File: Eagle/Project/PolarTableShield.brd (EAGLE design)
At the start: 56 x 59.7 mm, 48 parts, among them IC1 74AHC1G86DBV, IC2 LM358D, J1 Pi Power Jack, J10 LED + Radio, J2 Header - Right angled, female, J3 Pi Connection, J5 IR Sensors, J6 Switch A + B, J7 Switch C + D, J8 Switch E + F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

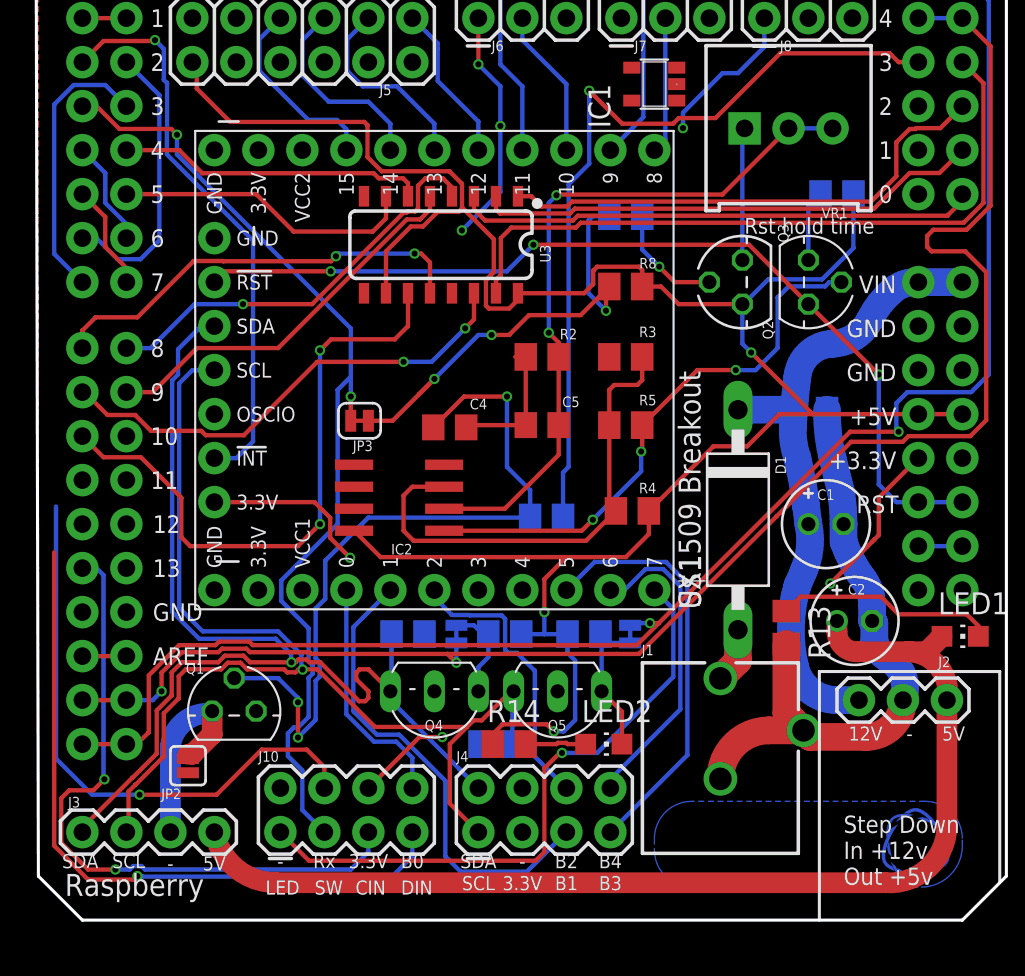
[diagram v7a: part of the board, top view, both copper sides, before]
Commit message: Moved the pins to be more efficient.
Put the rotory encoder signals onto D8 & D9 so they are on digital pin bank B in the lowest two bits. This can save a cycle shifting the data into position.
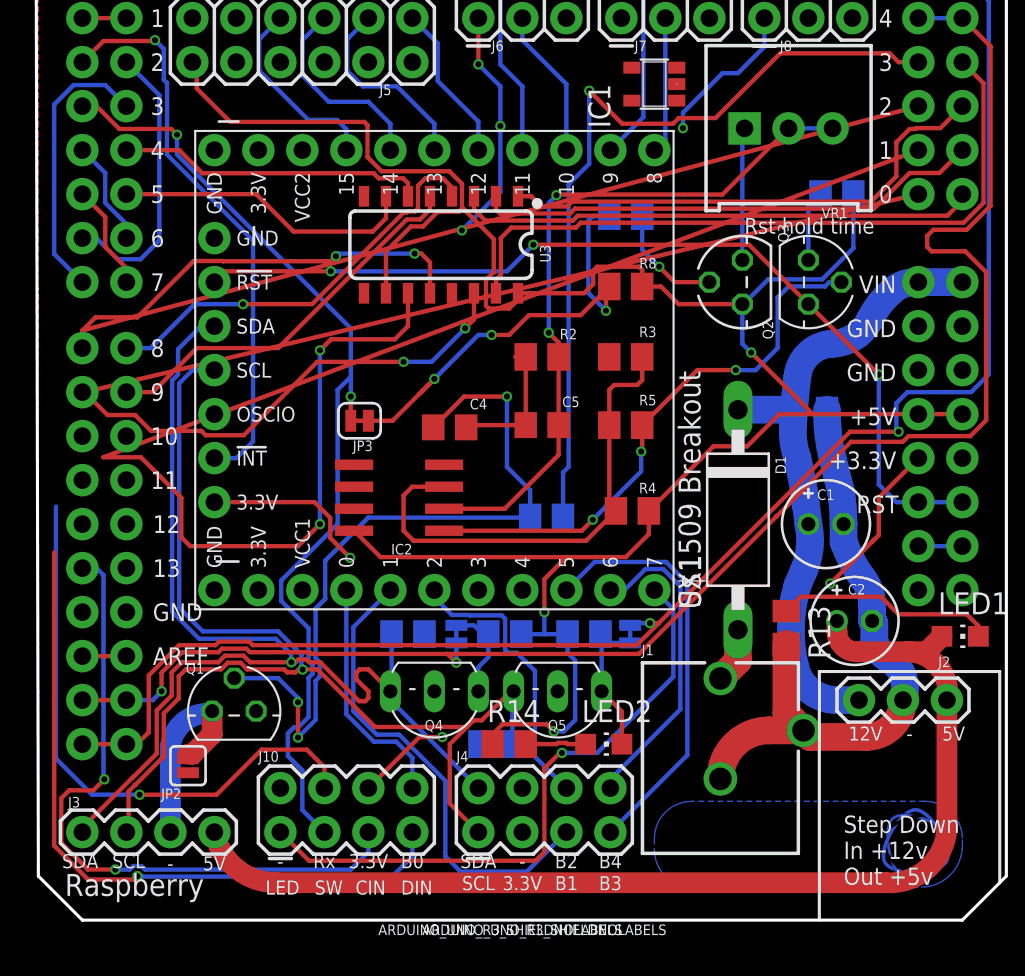
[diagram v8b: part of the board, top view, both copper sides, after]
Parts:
- B1, B2: value (none) -> ARDUINO_UNO_R3_SHIELDNOLABELS
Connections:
- net D11_SDIN renamed SDIN
- net D12_RXDATA renamed RXDATA
- net D13_SCIN renamed SCIN
- removed net A0_SW_E: B1.A0, IC1.1, J8.3
- removed net A1_SW_F: B1.A1, IC1.2, J8.4
- removed net A2_WAKE_SW: B1.A2, B1.D3, IC1.4, J10.3, JP3.1
- new net SW_E: B1.D8, IC1.1, J8.3
- new net SW_F: B1.D9, IC1.2, J8.4
- new net WAKE_SW: B1.D10, B1.D3, IC1.4, J10.3, JP3.1
- net CLK: now also B1.A1; no longer B1.D10
- net DATA: now also B1.A0; no longer B1.D9
- net LATCH: now also B1.A2; no longer B1.D8
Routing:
- net WAKE_SW: track 0.00 -> 56.3 mm, vias 0 -> 2
- net A2_WAKE_SW: track 56.3 -> 0.00 mm, vias 2 -> 0
- net DATA: track 27.9 -> 77.3 mm
- net LATCH: track 24.9 -> 73.9 mm
- net CLK: track 35.8 -> 84.3 mm
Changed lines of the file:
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@@
 </autorouter>
 <elements>
-<element name="B1" library="keir_library" package="UNO_R3_SHIELD_NOLABELS" package3d_urn="urn:adsk.eagle:package:37324/1" value="" x="26.67" y="30.48"/>
+<element name="B1" library="keir_library" package="UNO_R3_SHIELD_NOLABELS" package3d_urn="urn:adsk.eagle:package:37324/1" value="ARDUINO_UNO_R3_SHIELDNOLABELS" x="26.67" y="30.48"/>
 <element name="J1" library="SparkFun-Connectors" library_urn="urn:adsk.eagle:library:513" package="POWER_JACK_PTH_BREAD" package3d_urn="urn:adsk.eagle:package:38228/1" value="Pi Power Jack" x="39.37" y="0.254">
 <attribute name="NAME" x="34.8234" y="15.2908" size="0.6096" layer="25" font="vector" ratio="18"/>
@@
 <attribute name="VALUE" x="29.718" y="21.59" size="0.6" layer="28" font="vector" ratio="18" rot="MR0"/>
 </element>
-<element name="B2" library="keir_library" package="UNO_R3_SHIELD_NOLABELS" package3d_urn="urn:adsk.eagle:package:37324/1" value="" x="29.21" y="30.48"/>
+<element name="B2" library="keir_library" package="UNO_R3_SHIELD_NOLABELS" package3d_urn="urn:adsk.eagle:package:37324/1" value="ARDUINO_UNO_R3_SHIELDNOLABELS" x="29.21" y="30.48"/>
 <element name="C4" library="resistor" library_urn="urn:adsk.eagle:library:348" package="C0805" package3d_urn="urn:adsk.eagle:package:23617/2" value="100nF" x="23.749" y="28.448">
 <attribute name="NAME" x="25.908" y="30.099" size="0.6096" layer="25" font="vector" ratio="18" rot="R180"/>
@@
 <wire x1="29.3497" y1="11.303" x2="29.7561" y2="10.8966" width="0.254" layer="1"/>
 </signal>
-<signal name="A2_WAKE_SW" class="4">
+<signal name="WAKE_SW" class="4">
 <contactref element="J10" pad="3"/>
 <contactref element="JP3" pad="1"/>
@@
 <wire x1="14.4046" y1="10.781825" x2="14.4046" y2="9.4714" width="0.254" layer="16"/>
 <wire x1="15.5956" y1="13.9830625" x2="15.5956" y2="11.7253375" width="0.254" layer="16"/>
-<contactref element="B1" pad="A2"/>
 <contactref element="B1" pad="D3"/>
 <contactref element="IC1" pad="4"/>
-<wire x1="34.26" y1="49.21" x2="50.8" y2="46.99" width="0" layer="19" extent="1-1"/>
+<wire x1="34.26" y1="49.21" x2="2.54" y2="27.94" width="0" layer="19" extent="1-1"/>
 <wire x1="18.034" y1="34.163" x2="34.26" y2="49.21" width="0" layer="19" extent="1-16"/>
 <wire x1="2.54" y1="46.99" x2="3.3557875" y2="46.99" width="0" layer="19" extent="1-1"/>
+<contactref element="B1" pad="D10"/>
 </signal>
 <signal name="PI_GROUND" class="2">
@@
 <signal name="CLK" class="4">
 <contactref element="U3" pad="11"/>
-<contactref element="B1" pad="D10"/>
-<wire x1="2.54" y1="27.94" x2="3.7592" y2="26.7208" width="0.254" layer="1"/>
+<wire x1="50.8" y1="44.45" x2="3.7592" y2="26.7208" width="0.254" layer="1"/>
 <wire x1="8.255" y1="24.384" x2="8.255" y2="22.098" width="0.254" layer="1"/>
 <wire x1="5.9182" y1="26.7208" x2="8.255" y2="24.384" width="0.254" layer="1"/>
@@
 <via x="16.256" y="32.893" extent="1-16" drill="0.35"/>
 <wire x1="20.574" y1="33.528" x2="16.891" y2="33.528" width="0.254" layer="1"/>
+<contactref element="B1" pad="A1"/>
 </signal>
 <signal name="XSTEP" class="4">
@@
 <signal name="LATCH" class="4">
 <contactref element="U3" pad="12"/>
-<contactref element="B1" pad="D8"/>
 <wire x1="22.606" y1="36.189" x2="22.606" y2="37.973" width="0.254" layer="1"/>
 <wire x1="22.606" y1="37.973" x2="22.098" y2="38.481" width="0.254" layer="1"/>
 <wire x1="22.098" y1="38.481" x2="21.717" y2="38.481" width="0.254" layer="1"/>
-<wire x1="2.54" y1="33.02" x2="2.54" y2="34.036" width="0.254" layer="1"/>
+<wire x1="50.8" y1="46.99" x2="2.54" y2="34.036" width="0.254" layer="1"/>
 <wire x1="2.54" y1="34.036" x2="3.302" y2="34.798" width="0.254" layer="1"/>
 <wire x1="5.715" y1="34.798" x2="3.302" y2="34.798" width="0.254" layer="1"/>
@@
 <wire x1="21.717" y1="38.481" x2="17.332225" y2="38.481" width="0.254" layer="16"/>
 <wire x1="17.332225" y1="38.481" x2="17.1751125" y2="38.3238875" width="0.254" layer="16"/>
+<contactref element="B1" pad="A2"/>
 </signal>
 <signal name="DATA" class="4">
 <contactref element="U3" pad="14"/>
-<contactref element="B1" pad="D9"/>
 <wire x1="6.4994125" y1="28.2448" x2="5.5850125" y2="29.1592" width="0.254" layer="1"/>
-<wire x1="2.667" y1="30.48" x2="2.54" y2="30.48" width="0.254" layer="1"/>
+<wire x1="2.667" y1="30.48" x2="50.8" y2="41.91" width="0.254" layer="1"/>
 <wire x1="25.146" y1="36.189" x2="25.146" y2="34.671" width="0.254" layer="1"/>
 <wire x1="5.5850125" y1="29.1592" x2="3.9878" y2="29.1592" width="0.254" layer="1"/>
@@
 <wire x1="24.638" y1="34.163" x2="22.7028875" y2="32.2278875" width="0.254" layer="16"/>
 <wire x1="22.7028875" y1="32.2278875" x2="21.082" y2="32.2278875" width="0.254" layer="16"/>
-</signal>
-<signal name="D12_RXDATA" class="4">
+<contactref element="B1" pad="A0"/>
+</signal>
+<signal name="RXDATA" class="4">
 <wire x1="1.016" y1="23.876" x2="1.016" y2="9.3247875" width="0.254" layer="16"/>
 <wire x1="1.016" y1="9.3247875" x2="3.1017875" y2="7.239" width="0.254" layer="16"/>
@@
 <wire x1="1.016" y1="23.876" x2="2.54" y2="22.86" width="0" layer="19" extent="16-16"/>
 </signal>
-<signal name="D13_SCIN" class="4">
+<signal name="SCIN" class="4">
 <contactref element="B1" pad="D13"/>
 <contactref element="J10" pad="5"/>
@@
 <wire x1="48.26" y1="17.145" x2="48.26" y2="16.129" width="1.6" layer="16"/>
 </signal>
-<signal name="A0_SW_E" class="4">
-<contactref element="B1" pad="A0"/>
+<signal name="SW_E" class="4">
 <contactref element="J8" pad="3"/>
 <contactref element="IC1" pad="1"/>
 <wire x1="36.85" y1="47.31" x2="44.45" y2="52.07" width="0" layer="19" extent="1-1"/>
-<wire x1="50.8" y1="41.91" x2="44.45" y2="52.07" width="0" layer="19" extent="1-1"/>
-</signal>
-<signal name="A1_SW_F" class="4">
-<contactref element="B1" pad="A1"/>
+<wire x1="2.54" y1="33.02" x2="44.45" y2="52.07" width="0" layer="19" extent="1-1"/>
+<contactref element="B1" pad="D8"/>
+</signal>
+<signal name="SW_F" class="4">
 <contactref element="J8" pad="4"/>
 <contactref element="IC1" pad="2"/>
 <wire x1="36.85" y1="48.26" x2="44.45" y2="54.61" width="0" layer="19" extent="1-1"/>
-<wire x1="50.8" y1="44.45" x2="44.45" y2="54.61" width="0" layer="19" extent="1-1"/>
+<wire x1="2.54" y1="30.48" x2="44.45" y2="54.61" width="0" layer="19" extent="1-1"/>
+<contactref element="B1" pad="D9"/>
 </signal>
 <signal name="A2" class="4">
@@
 <wire x1="29.911775" y1="10.16" x2="28.128" y2="10.16" width="0.254" layer="1"/>
 </signal>
-<signal name="D11_SDIN">
+<signal name="SDIN">
 <contactref element="B1" pad="D11"/>
 <contactref element="J10" pad="7"/>
